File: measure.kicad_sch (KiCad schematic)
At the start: 10 parts, among them SW1 SW_Push_SPDT, SW2 SW_Push_SPDT, U1 ATtiny85-20S, U2 INA226, U3 L7805

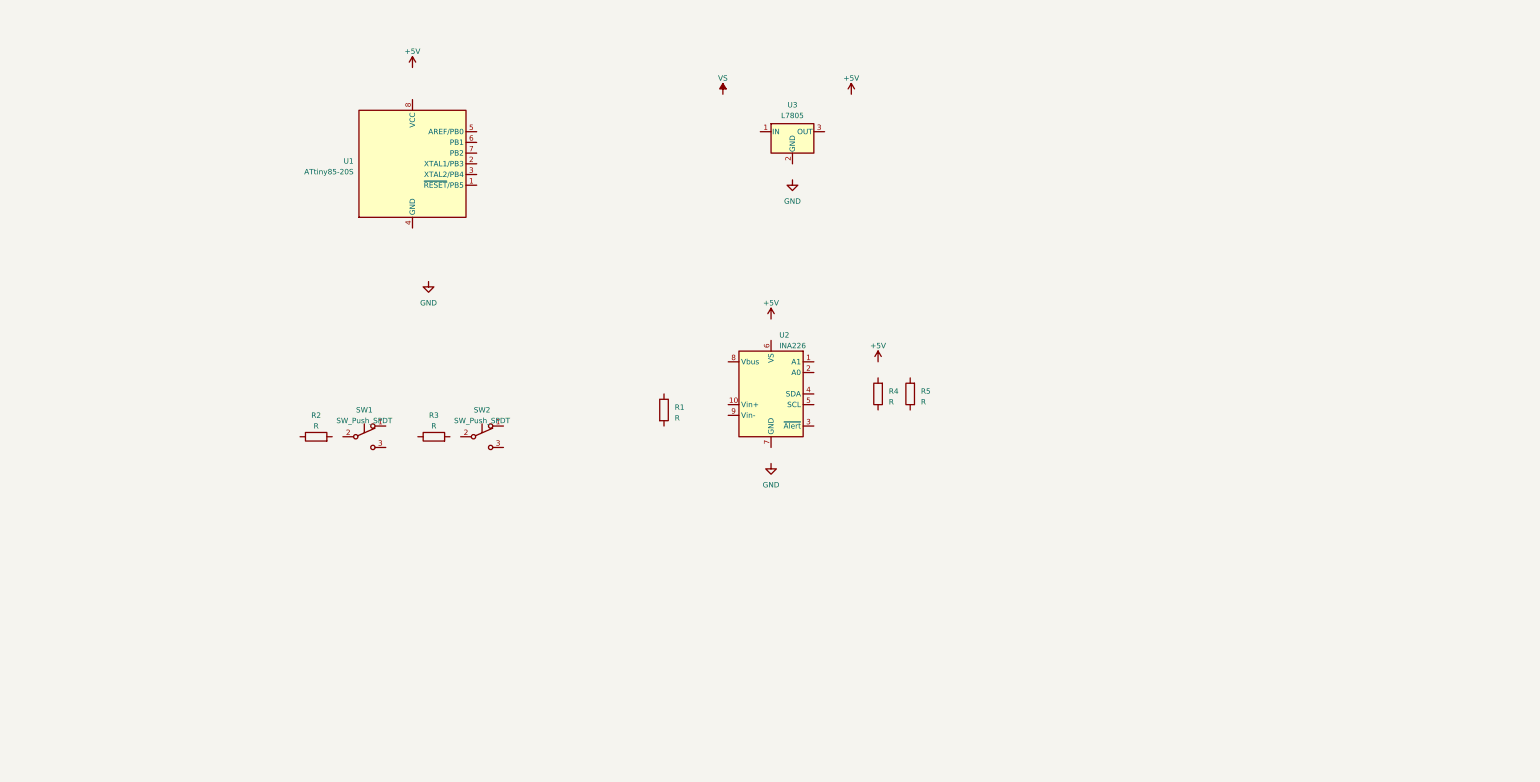
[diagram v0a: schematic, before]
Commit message: component placement
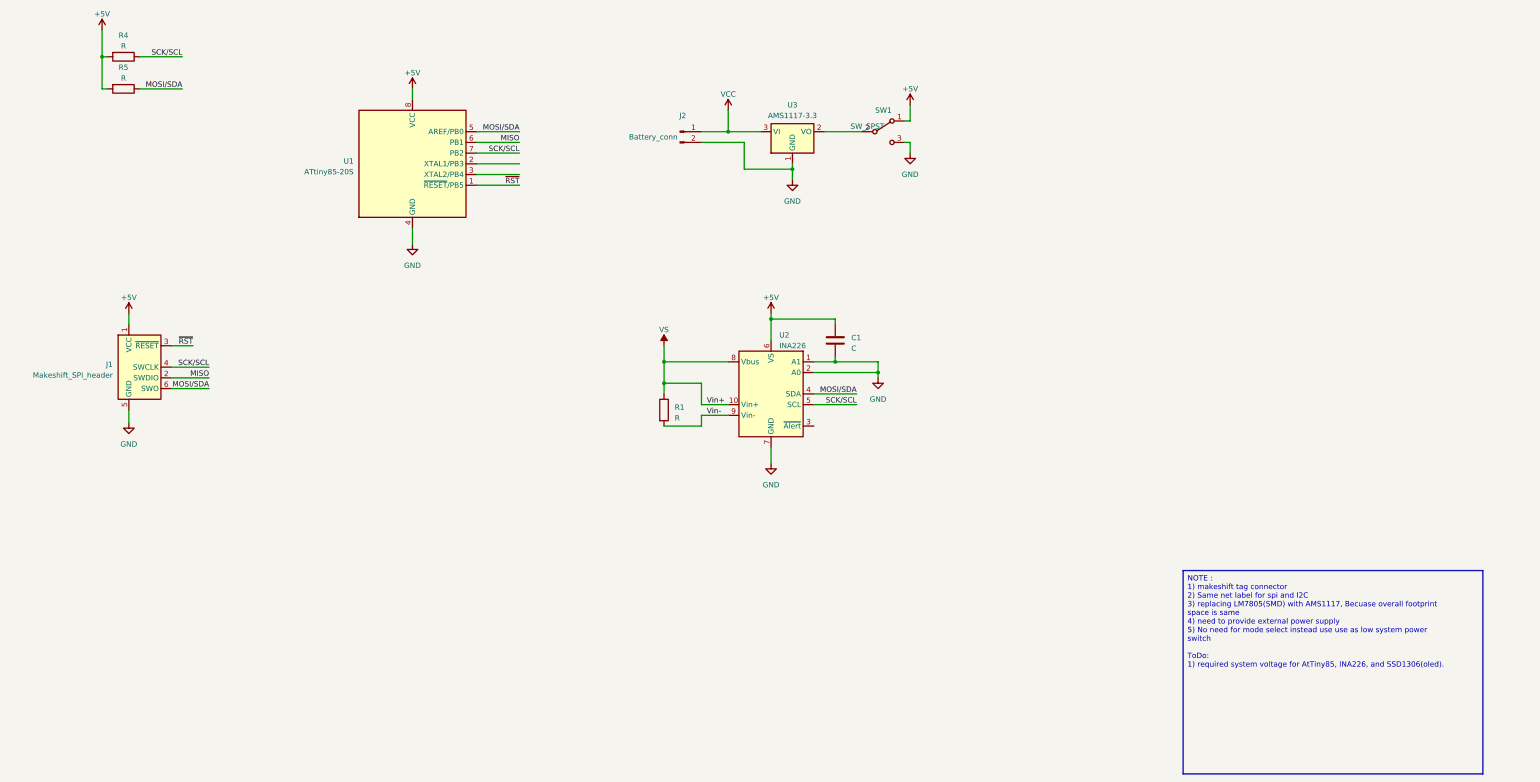
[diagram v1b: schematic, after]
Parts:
- removed R2, R3: R, Resistor_SMD:R_0805_2012Metric, symbol Device:R
- removed SW1, SW2: SW_Push_SPDT, Button_Switch_SMD:SW_SPDT_CK-JS102011SAQN, symbol Switch:SW_Push_SPDT
- removed U3: L7805, Package_TO_SOT_SMD:TO-252-2, symbol Regulator_Linear:L7805
- added C1: C, Capacitor_SMD:C_0805_2012Metric, symbol Device:C
- added J1: Makeshift_SPI_header, Connector:Tag-Connect_TC2030-IDC-NL_2x03_P1.27mm_Vertical, symbol Connector:Conn_ARM_SWD_TagConnect_TC2030-NL
- added J2: Battery_conn, Connector_JST:JST_GH_SM02B-GHS-TB_1x02-1MP_P1.25mm_Horizontal, symbol Connector:Conn_01x02_Pin
- added SW1: SW_SPST, Button_Switch_SMD:SW_SPDT_CK-JS102011SAQN, symbol Switch:SW_SPDT
- added U3: AMS1117-3.3, Package_TO_SOT_SMD:SOT-223-3_TabPin2, symbol Regulator_Linear:AMS1117-3.3
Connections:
- net +5V: now also R4.2, R5.2, U1.8 (VCC), U2.6 (VS), C1.1, J1.1 (VCC), SW1.1 (A)
- net GND: now also U1.4 (GND), U2.1 (A1), U2.2 (A0), U2.7 (GND), C1.2, J1.5 (GND), J2.2 (Pin_2), SW1.3 (C), U3.1 (GND)
- net VS: now also R1.1, U2.10 (Vin+), U2.8 (Vbus)
- net MOSI/SDA: now reaches R5.1
- net MOSI/SDA: now also U1.5 (AREF/PB0), U2.4 (SDA), J1.6 (SWO)
- net Vin-: now reaches R1.2
- net Vin-: now also U2.9 (Vin-)
- net ~{RST}: now reaches U1.1 (~{RESET}/PB5)
- net ~{RST}: now also J1.3 (~{RESET})
- net MISO: now reaches U1.6 (PB1)
- net MISO: now also J1.2 (SWDIO)
- net SCK/SCL: now reaches U1.7 (PB2)
- net SCK/SCL: now also R4.1, U2.5 (SCL), J1.4 (SWCLK)
- new net: SW1.2 (B), U3.2 (VO)
- new net VCC: J2.1 (Pin_1), U3.3 (VI)
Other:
- moved on the sheet: R4, R5

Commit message: Shunt looks good
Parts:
- added TP1: IN, TestPoint:TestPoint_Pad_4.0x4.0mm, symbol Connector:TestPoint
- added TP2: OUT, TestPoint:TestPoint_Pad_4.0x4.0mm, symbol Connector:TestPoint
- R4, R5: footprint Resistor_SMD:R_0805_2012Metric -> Resistor_SMD:R_0603_1608Metric
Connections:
- net MISO: now also J1.4 (SWCLK); no longer J1.2 (SWDIO)
- net MOSI/SDA: now also J1.2 (SWDIO); no longer J1.6 (SWO)
- net SCK/SCL: now also J1.6 (SWO); no longer J1.4 (SWCLK)
- net Vin-: now also TP2.1
- net VS renamed Vin+
- net Vin+: now also TP1.1
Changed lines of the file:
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@@
   (junction (at 201.93 100.33) (diameter 0) (color 0 0 0 0)
   )
-  (junction (at 176.53 110.49) (diameter 0) (color 0 0 0 0)
-  )
   (junction (at 43.18 38.1) (diameter 0) (color 0 0 0 0)
   )
@@
   (junction (at 207.01 64.77) (diameter 0) (color 0 0 0 0)
   )
+  (junction (at 176.53 127) (diameter 0) (color 0 0 0 0)
+  )
   (junction (at 176.53 115.57) (diameter 0) (color 0 0 0 0)
   )
@@
     (stroke (width 0) (type default))
   )
+  (wire (pts (xy 170.18 115.57) (xy 176.53 115.57))
+    (stroke (width 0) (type default))
+  )
   (wire (pts (xy 132.08 66.04) (xy 142.24 66.04))
     (stroke (width 0) (type default))
@@
     (stroke (width 0) (type default))
   )
-  (wire (pts (xy 176.53 125.73) (xy 185.42 125.73))
+  (wire (pts (xy 176.53 127) (xy 185.42 127))
+    (stroke (width 0) (type default))
+  )
+  (wire (pts (xy 170.18 127) (xy 170.18 130.81))
     (stroke (width 0) (type default))
   )
@@
     (stroke (width 0) (type default))
   )
-  (wire (pts (xy 185.42 125.73) (xy 185.42 123.19))
+  (wire (pts (xy 185.42 127) (xy 185.42 123.19))
     (stroke (width 0) (type default))
   )
@@
     (stroke (width 0) (type default))
   )
+  (wire (pts (xy 170.18 127) (xy 176.53 127))
+    (stroke (width 0) (type default))
+  )
   (wire (pts (xy 59.69 106.68) (xy 64.77 106.68))
     (stroke (width 0) (type default))
@@
     (stroke (width 0) (type default))
   )
+  (wire (pts (xy 176.53 127) (xy 176.53 125.73))
+    (stroke (width 0) (type default))
+  )
   (wire (pts (xy 212.09 113.03) (xy 227.33 113.03))
     (stroke (width 0) (type default))
@@
     (stroke (width 0) (type default))
   )
-  (wire (pts (xy 176.53 106.68) (xy 176.53 110.49))
-    (stroke (width 0) (type default))
-  )
   (wire (pts (xy 212.09 120.65) (xy 222.25 120.65))
     (stroke (width 0) (type default))
@@
     (stroke (width 0) (type default))
   )
+  (wire (pts (xy 170.18 111.76) (xy 170.18 115.57))
+    (stroke (width 0) (type default))
+  )
   (image (at -81.28 82.55) (scale 2.63334)
     (data
@@
     (effects (font (size 1.27 1.27)) (justify left bottom))
   )
-  (label "MOSI{slash}SDA" (at 68.58 116.84 180) (fields_autoplaced)
+  (label "MOSI{slash}SDA" (at 68.58 114.3 180) (fields_autoplaced)
     (effects (font (size 1.27 1.27)) (justify right bottom))
   )
@@
     (effects (font (size 1.27 1.27)) (justify right bottom))
   )
-  (label "SCK{slash}SCL" (at 68.58 111.76 180) (fields_autoplaced)
+  (label "SCK{slash}SCL" (at 68.58 116.84 180) (fields_autoplaced)
     (effects (font (size 1.27 1.27)) (justify right bottom))
   )
@@
     (effects (font (size 1.27 1.27)) (justify right bottom))
   )
-  (label "MISO" (at 68.58 114.3 180) (fields_autoplaced)
+  (label "MISO" (at 68.58 111.76 180) (fields_autoplaced)
     (effects (font (size 1.27 1.27)) (justify right bottom))
   )
@@
     )
   )
+  (symbol (lib_id "Connector:TestPoint") (at 170.18 111.76 0) (unit 1)
+    (in_bom yes) (on_board yes) (dnp no) (fields_autoplaced)
+    (property "Reference" "TP1" (at 172.72 107.823 0)
+      (effects (font (size 1.27 1.27)) (justify left))
+    )
+    (property "Value" "IN" (at 172.72 110.363 0)
+      (effects (font (size 1.27 1.27)) (justify left))
+    )
+    (property "Footprint" "TestPoint:TestPoint_Pad_4.0x4.0mm" (at 175.26 111.76 0)
+      (effects (font (size 1.27 1.27)) hide)
+    )
+    (property "Datasheet" "~" (at 175.26 111.76 0)
+      (effects (font (size 1.27 1.27)) hide)
+    )
+    (pin "1")
+    (instances
+      (project "measure"
+        (path "/135129c2-76df-4afe-bb76-10cf805e8524"
+          (reference "TP1") (unit 1)
+        )
+      )
+    )
+  )
   (symbol (lib_id "power:+5V") (at 201.93 99.06 0) (unit 1)
     (in_bom yes) (on_board yes) (dnp no) (fields_autoplaced)
@@
     )
   )
+  (symbol (lib_id "Connector:TestPoint") (at 170.18 130.81 180) (unit 1)
+    (in_bom yes) (on_board yes) (dnp no) (fields_autoplaced)
+    (property "Reference" "TP2" (at 172.72 133.477 0)
+      (effects (font (size 1.27 1.27)) (justify right))
+    )
+    (property "Value" "OUT" (at 172.72 136.017 0)
+      (effects (font (size 1.27 1.27)) (justify right))
+    )
+    (property "Footprint" "TestPoint:TestPoint_Pad_4.0x4.0mm" (at 165.1 130.81 0)
+      (effects (font (size 1.27 1.27)) hide)
+    )
+    (property "Datasheet" "~" (at 165.1 130.81 0)
+      (effects (font (size 1.27 1.27)) hide)
+    )
+    (pin "1")
+    (instances
+      (project "measure"
+        (path "/135129c2-76df-4afe-bb76-10cf805e8524"
+          (reference "TP2") (unit 1)
+        )
+      )
+    )
+  )
   (symbol (lib_id "Device:R") (at 48.26 45.72 270) (unit 1)
     (in_bom yes) (on_board yes) (dnp no) (fields_autoplaced)
@@
       (effects (font (size 1.27 1.27)))
     )
-    (property "Footprint" "Resistor_SMD:R_0805_2012Metric" (at 48.26 43.942 90)
+    (property "Footprint" "Resistor_SMD:R_0603_1608Metric" (at 48.26 43.942 90)
       (effects (font (size 1.27 1.27)) hide)
     )
@@
     )
   )
-  (symbol (lib_id "power:VS") (at 176.53 106.68 0) (unit 1)
-    (in_bom yes) (on_board yes) (dnp no) (fields_autoplaced)
-    (property "Reference" "#PWR014" (at 171.45 110.49 0)
-      (effects (font (size 1.27 1.27)) hide)
-    )
-    (property "Value" "VS" (at 176.53 102.87 0)
-      (effects (font (size 1.27 1.27)))
-    )
-    (property "Footprint" "" (at 176.53 106.68 0)
-      (effects (font (size 1.27 1.27)) hide)
-    )
-    (property "Datasheet" "" (at 176.53 106.68 0)
-      (effects (font (size 1.27 1.27)) hide)
-    )
-    (pin "1")
-    (instances
-      (project "measure"
-        (path "/135129c2-76df-4afe-bb76-10cf805e8524"
-          (reference "#PWR014") (unit 1)
-        )
-      )
-    )
-  )
   (symbol (lib_id "power:GND") (at 207.01 67.31 0) (unit 1)
     (in_bom yes) (on_board yes) (dnp no) (fields_autoplaced)
@@
       (effects (font (size 1.27 1.27)))
     )
-    (property "Footprint" "Resistor_SMD:R_0805_2012Metric" (at 48.26 36.322 90)
+    (property "Footprint" "Resistor_SMD:R_0603_1608Metric" (at 48.26 36.322 90)
       (effects (font (size 1.27 1.27)) hide)
     )

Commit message: Lets name it tinyzinger
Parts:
- added U4: SSD1306_OLEDModule, sche:SSD1306_OLEDModule, symbol sche:SSD1306_oledmodule
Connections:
- net GND: now also U4.1 (GND)
- net MOSI/SDA: now also U4.4 (SDA)
- net SCK/SCL: now also U4.3 (SCL)
- net +5V renamed +3V3
- net +3V3: now also U4.2 (Vcc)
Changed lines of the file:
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@@
     (stroke (width 0) (type default))
   )
+  (wire (pts (xy 146.05 157.48) (xy 146.05 161.29))
+    (stroke (width 0) (type default))
+  )
   (wire (pts (xy 227.33 110.49) (xy 227.33 113.03))
     (stroke (width 0) (type default))
@@
     (stroke (width 0) (type default))
   )
+  (wire (pts (xy 156.21 149.86) (xy 166.37 149.86))
+    (stroke (width 0) (type default))
+  )
+  (wire (pts (xy 156.21 144.78) (xy 165.1 144.78))
+    (stroke (width 0) (type default))
+  )
   (wire (pts (xy 212.09 110.49) (xy 217.17 110.49))
     (stroke (width 0) (type default))
@@
     (stroke (width 0) (type default))
   )
+  (wire (pts (xy 146.05 133.35) (xy 146.05 137.16))
+    (stroke (width 0) (type default))
+  )
   (wire (pts (xy 59.69 116.84) (xy 68.58 116.84))
     (stroke (width 0) (type default))
@@
     (stroke (width 0) (type default))
   )
-  (image (at -81.28 82.55) (scale 2.63334)
+  (image (at -53.34 71.12) (scale 1.684)
     (data
       iVBORw0KGgoAAAANSUhEUgAAAtIAAAEOCAIAAAArHGc0AAAAA3NCSVQICAjb4U/gAAAgAElEQVR4
@@
     )
   )
-  (text_box "NOTE : \n1) makeshift tag connector\n2) Same net label for spi and I2C\n3) replacing LM7805(SMD) with AMS1117, Becuase overall footprint space is same\n4) need to provide external power supply\n5) No need for mode select instead use use as low system power switch \n\nToDo:\n1) required system voltage for AtTiny85, INA226, and SSD1306(oled)."
+  (text_box "NOTE : \n1) makeshift tag connector(-)\n2) Same net label for spi and I2C(NP)\n3) replacing LM7805(SMD) with AMS1117, Becuase overall footprint space is same\n4) need to provide external power supply(-)\n5) No need for mode select instead use as system power switch(-) \n\nToDo:\n1) required system voltage for AtTiny85, INA226, and SSD1306(oled)."
     (at 299.72 160.02 0) (size 71.12 48.26)
     (stroke (width 0) (type default))
@@
     (effects (font (size 1.27 1.27)) (justify right bottom))
   )
+  (label "MOSI{slash}SDA" (at 166.37 149.86 180) (fields_autoplaced)
+    (effects (font (size 1.27 1.27)) (justify right bottom))
+  )
+  (label "SCK{slash}SCL" (at 165.1 144.78 180) (fields_autoplaced)
+    (effects (font (size 1.27 1.27)) (justify right bottom))
+  )
   (label "MOSI{slash}SDA" (at 222.25 118.11 180) (fields_autoplaced)
     (effects (font (size 1.27 1.27)) (justify right bottom))
@@
     )
   )
-  (symbol (lib_id "power:+5V") (at 43.18 31.75 0) (unit 1)
+  (symbol (lib_id "power:+3V3") (at 43.18 31.75 0) (unit 1)
     (in_bom yes) (on_board yes) (dnp no) (fields_autoplaced)
-    (property "Reference" "#PWR08" (at 43.18 35.56 0)
+    (property "Reference" "#PWR0103" (at 43.18 35.56 0)
       (effects (font (size 1.27 1.27)) hide)
     )
-    (property "Value" "+5V" (at 43.18 27.94 0)
+    (property "Value" "+3V3" (at 43.18 28.194 0)
       (effects (font (size 1.27 1.27)))
     )
@@
       (project "measure"
         (path "/135129c2-76df-4afe-bb76-10cf805e8524"
-          (reference "#PWR08") (unit 1)
+          (reference "#PWR0103") (unit 1)
         )
       )
     )
   )
-  (symbol (lib_id "power:+5V") (at 116.84 45.72 0) (unit 1)
+  (symbol (lib_id "power:+3V3") (at 116.84 45.72 0) (unit 1)
     (in_bom yes) (on_board yes) (dnp no) (fields_autoplaced)
-    (property "Reference" "#PWR02" (at 116.84 49.53 0)
+    (property "Reference" "#PWR0105" (at 116.84 49.53 0)
       (effects (font (size 1.27 1.27)) hide)
     )
-    (property "Value" "+5V" (at 116.84 41.91 0)
+    (property "Value" "+3V3" (at 116.84 42.164 0)
       (effects (font (size 1.27 1.27)))
     )
@@
       (project "measure"
         (path "/135129c2-76df-4afe-bb76-10cf805e8524"
-          (reference "#PWR02") (unit 1)
+          (reference "#PWR0105") (unit 1)
         )
       )
@@
     )
   )
-  (symbol (lib_id "power:+5V") (at 201.93 99.06 0) (unit 1)
+  (symbol (lib_id "power:+3V3") (at 201.93 99.06 0) (unit 1)
     (in_bom yes) (on_board yes) (dnp no) (fields_autoplaced)
-    (property "Reference" "#PWR05" (at 201.93 102.87 0)
+    (property "Reference" "#PWR0101" (at 201.93 102.87 0)
       (effects (font (size 1.27 1.27)) hide)
     )
-    (property "Value" "+5V" (at 201.93 95.25 0)
+    (property "Value" "+3V3" (at 201.93 95.504 0)
       (effects (font (size 1.27 1.27)))
     )
@@
       (project "measure"
         (path "/135129c2-76df-4afe-bb76-10cf805e8524"
-          (reference "#PWR05") (unit 1)
+          (reference "#PWR0101") (unit 1)
         )
       )
@@
     )
   )
-  (symbol (lib_id "power:+5V") (at 49.53 99.06 0) (unit 1)
+  (symbol (lib_id "power:+3V3") (at 49.53 99.06 0) (unit 1)
     (in_bom yes) (on_board yes) (dnp no) (fields_autoplaced)
-    (property "Reference" "#PWR010" (at 49.53 102.87 0)
+    (property "Reference" "#PWR0102" (at 49.53 102.87 0)
       (effects (font (size 1.27 1.27)) hide)
     )
-    (property "Value" "+5V" (at 49.53 95.25 0)
+    (property "Value" "+3V3" (at 49.53 95.504 0)
       (effects (font (size 1.27 1.27)))
     )
@@
       (project "measure"
         (path "/135129c2-76df-4afe-bb76-10cf805e8524"
-          (reference "#PWR010") (unit 1)
+          (reference "#PWR0102") (unit 1)
         )
       )
@@
     )
   )
+  (symbol (lib_id "sche:SSD1306_oledmodule") (at 146.05 147.32 0) (unit 1)
+    (in_bom yes) (on_board yes) (dnp no)
+    (property "Reference" "U4" (at 137.16 147.955 0)
+      (effects (font (size 1.27 1.27)) (justify right))
+    )
+    (property "Value" "SSD1306_OLEDModule" (at 128.27 151.13 0)
+      (effects (font (size 1.27 1.27)))
+    )
+    (property "Footprint" "sche:SSD1306_OLEDModule" (at 146.05 139.7 0)
+      (effects (font (size 1.27 1.27)) hide)
+    )
+    (property "Datasheet" "" (at 146.05 139.7 0)
+      (effects (font (size 1.27 1.27)) hide)
+    )
+    (pin "1")
+    (pin "2")
+    (pin "3")
+    (pin "4")
+    (instances
+      (project "measure"
+        (path "/135129c2-76df-4afe-bb76-10cf805e8524"
+          (reference "U4") (unit 1)
+        )
+      )
+    )
+  )
   (symbol (lib_id "power:GND") (at 207.01 67.31 0) (unit 1)
     (in_bom yes) (on_board yes) (dnp no) (fields_autoplaced)
@@
     )
   )
-  (symbol (lib_id "power:+5V") (at 234.95 49.53 0) (unit 1)
+  (symbol (lib_id "power:+3V3") (at 234.95 49.53 0) (unit 1)
     (in_bom yes) (on_board yes) (dnp no) (fields_autoplaced)
-    (property "Reference" "#PWR04" (at 234.95 53.34 0)
+    (property "Reference" "#PWR0104" (at 234.95 53.34 0)
       (effects (font (size 1.27 1.27)) hide)
     )
-    (property "Value" "+5V" (at 234.95 45.72 0)
+    (property "Value" "+3V3" (at 234.95 45.974 0)
       (effects (font (size 1.27 1.27)))
     )
@@
       (project "measure"
         (path "/135129c2-76df-4afe-bb76-10cf805e8524"
-          (reference "#PWR04") (unit 1)
+          (reference "#PWR0104") (unit 1)
+        )
+      )
+    )
+  )
+  (symbol (lib_id "power:+3V3") (at 146.05 133.35 0) (unit 1)
+    (in_bom yes) (on_board yes) (dnp no) (fields_autoplaced)
+    (property "Reference" "#PWR0106" (at 146.05 137.16 0)
+      (effects (font (size 1.27 1.27)) hide)
+    )
+    (property "Value" "+3V3" (at 146.05 129.794 0)
+      (effects (font (size 1.27 1.27)))
+    )
+    (property "Footprint" "" (at 146.05 133.35 0)
+      (effects (font (size 1.27 1.27)) hide)
+    )
+    (property "Datasheet" "" (at 146.05 133.35 0)
+      (effects (font (size 1.27 1.27)) hide)
+    )
+    (pin "1")
+    (instances
+      (project "measure"
+        (path "/135129c2-76df-4afe-bb76-10cf805e8524"
+          (reference "#PWR0106") (unit 1)
         )
       )
@@
         )
       )
+    )
+  )
+  (symbol (lib_id "power:GND") (at 146.05 161.29 0) (unit 1)
+    (in_bom yes) (on_board yes) (dnp no) (fields_autoplaced)
+    (property "Reference" "#PWR013" (at 146.05 167.64 0)
+      (effects (font (size 1.27 1.27)) hide)
+    )
+    (property "Value" "GND" (at 146.05 166.37 0)
+      (effects (font (size 1.27 1.27)))
+    )
+    (property "Footprint" "" (at 146.05 161.29 0)
+      (effects (font (size 1.27 1.27)) hide)
+    )
+    (property "Datasheet" "" (at 146.05 161.29 0)
+      (effects (font (size 1.27 1.27)) hide)
+    )
+    (pin "1")
+    (instances
+      (project "measure"
+        (path "/135129c2-76df-4afe-bb76-10cf805e8524"
+          (reference "#PWR013") (unit 1)
+        )
+      )
